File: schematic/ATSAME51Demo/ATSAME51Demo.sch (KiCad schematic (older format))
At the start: 1 part

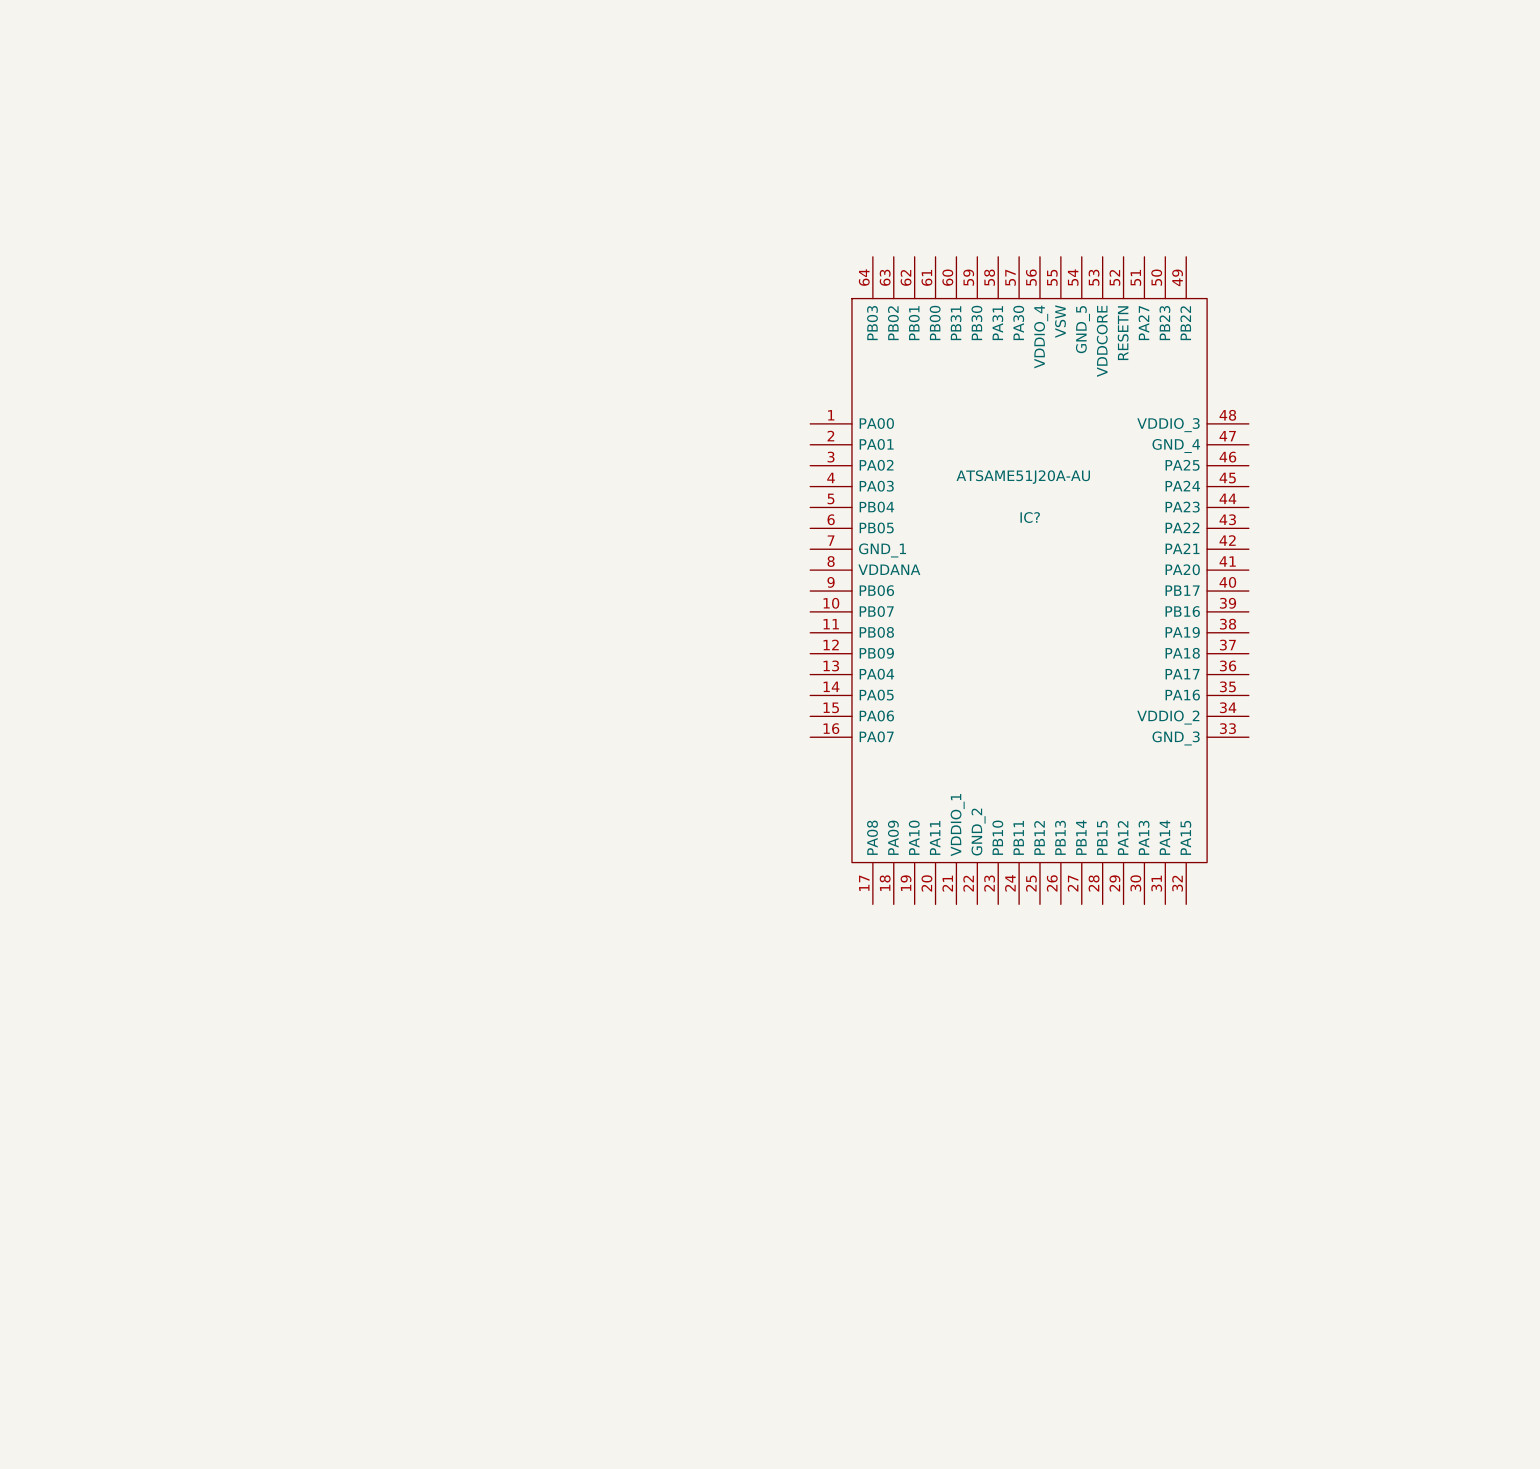
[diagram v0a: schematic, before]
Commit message: Schematic first draft
Still needs footprints
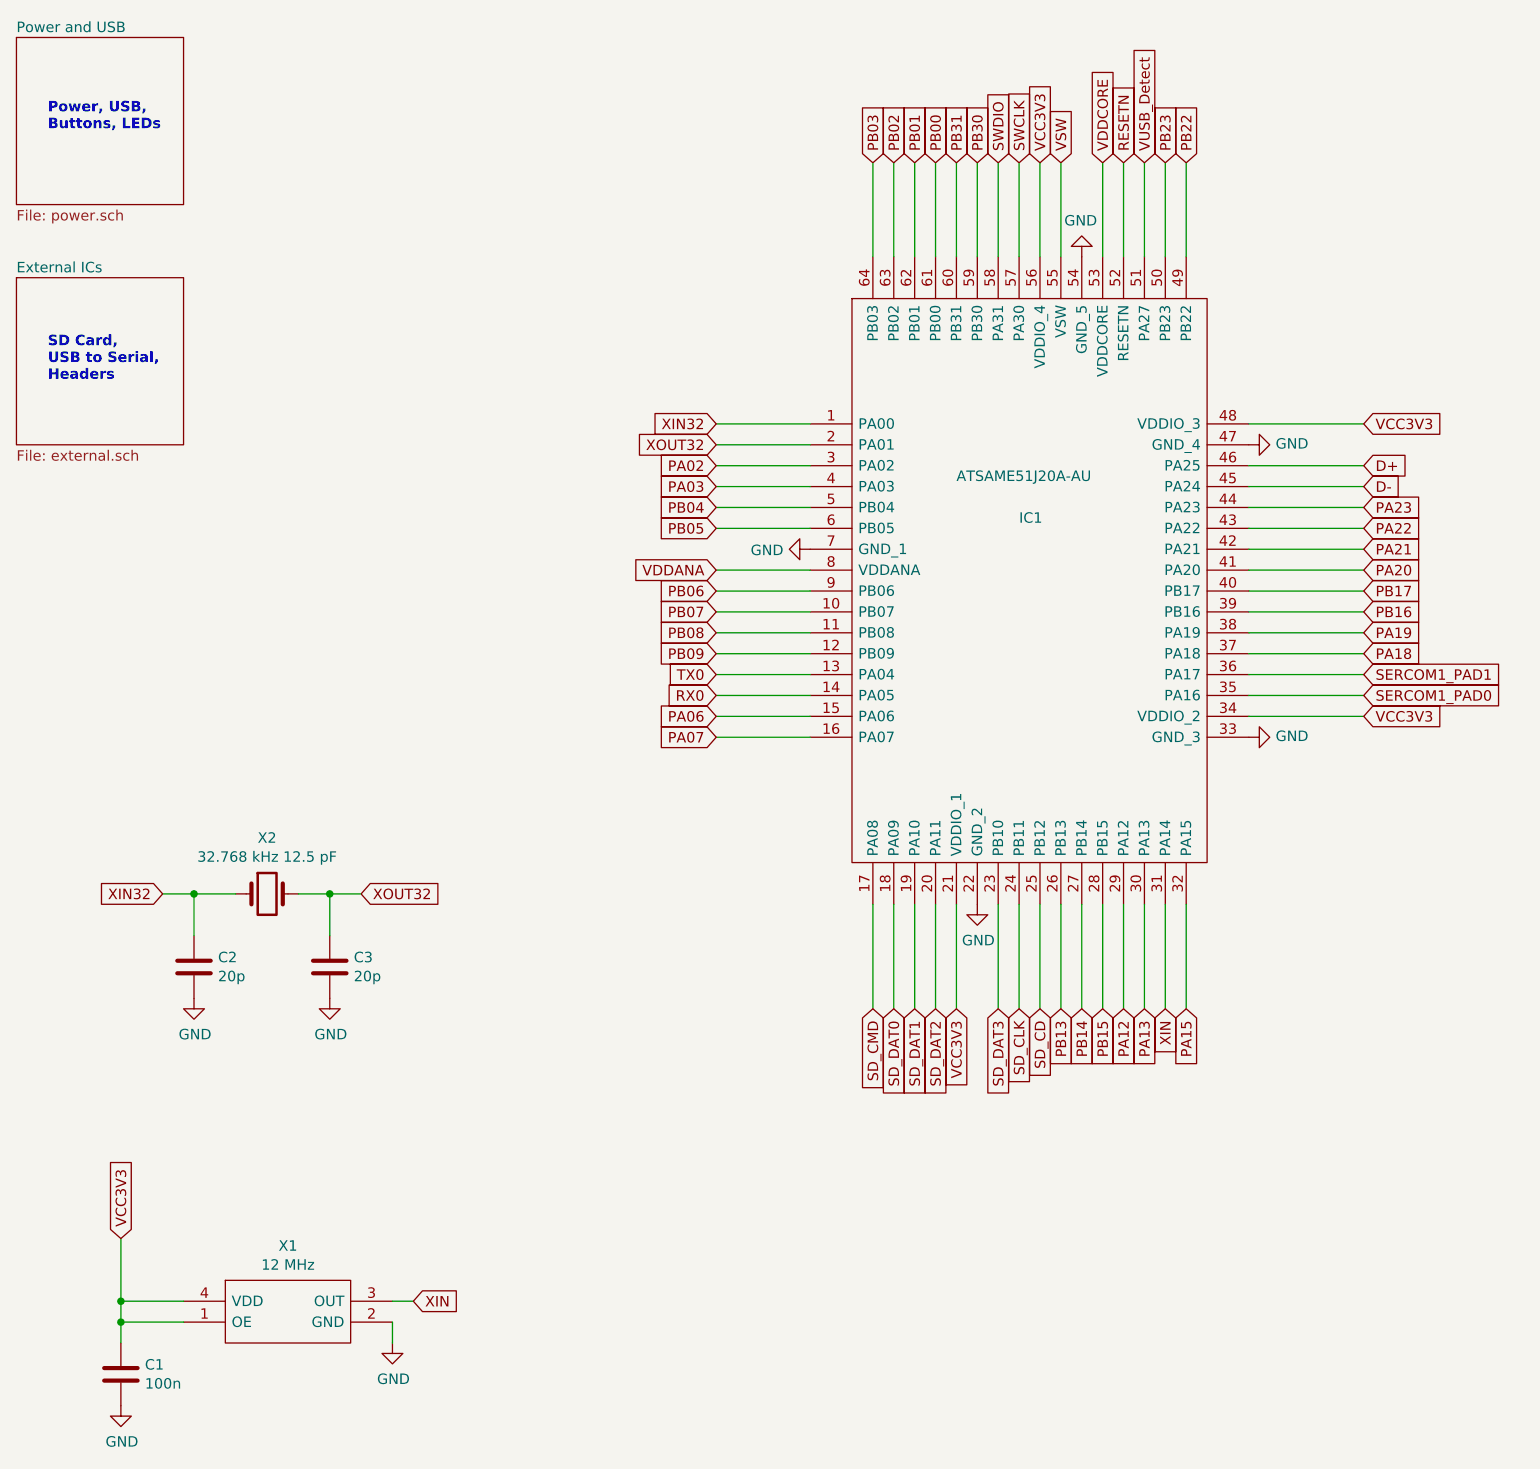
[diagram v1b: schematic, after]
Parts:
- added C1: 100n, symbol Device:C
- added C2, C3: 20p, symbol Device:C
- added X1: 12 MHz, SamacSys_Parts:ASTMUPCE3312000MHZLJET, symbol SamacSys_Parts:ASTMUPCE-33-12.000MHZ-LJ-E-T
- added X2: 32.768 kHz 12.5 pF, SamacSys_Parts:CM9VT1A, symbol Device:Crystal
- gave numbers to parts that had none: 1
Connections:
- net XIN32: now reaches IC1.1 (PA00)
- net XIN32: now also C2.1, X2.1
- net PB07: now reaches IC1.10 (PB07)
- net PB08: now reaches IC1.11 (PB08)
- net PB09: now reaches IC1.12 (PB09)
- net TX0: now reaches IC1.13 (PA04)
- net RX0: now reaches IC1.14 (PA05)
- net PA06: now reaches IC1.15 (PA06)
- net PA07: now reaches IC1.16 (PA07)
- net SD_CMD: now reaches IC1.17 (PA08)
- net SD_DAT0: now reaches IC1.18 (PA09)
- net SD_DAT1: now reaches IC1.19 (PA10)
- net XOUT32: now reaches IC1.2 (PA01)
- net XOUT32: now also C3.1, X2.2
- net SD_DAT2: now reaches IC1.20 (PA11)
- net VCC3V3: now reaches IC1.21 (VDDIO_1)
- net VCC3V3: now also IC1.34 (VDDIO_2), IC1.48 (VDDIO_3), IC1.56 (VDDIO_4), C1.1, X1.1 (OE), X1.4 (VDD)
- net GND: now reaches IC1.22 (GND_2)
- net GND: now also IC1.33 (GND_3), IC1.47 (GND_4), IC1.54 (GND_5), IC1.7 (GND_1), C1.2, C2.2, C3.2, X1.2 (GND)
- net SD_DAT3: now reaches IC1.23 (PB10)
- net SD_CLK: now reaches IC1.24 (PB11)
- net SD_CD: now reaches IC1.25 (PB12)
- net PB13: now reaches IC1.26 (PB13)
- net PB14: now reaches IC1.27 (PB14)
- net PB15: now reaches IC1.28 (PB15)
- net PA12: now reaches IC1.29 (PA12)
- net PA02: now reaches IC1.3 (PA02)
- net PA13: now reaches IC1.30 (PA13)
- net XIN: now reaches IC1.31 (PA14)
- net XIN: now also X1.3 (OUT)
- net PA15: now reaches IC1.32 (PA15)
- net SERCOM1_PAD0: now reaches IC1.35 (PA16)
- net SERCOM1_PAD1: now reaches IC1.36 (PA17)
- net PA18: now reaches IC1.37 (PA18)
- net PA19: now reaches IC1.38 (PA19)
- net PB16: now reaches IC1.39 (PB16)
- net PA03: now reaches IC1.4 (PA03)
- net PB17: now reaches IC1.40 (PB17)
- net PA20: now reaches IC1.41 (PA20)
- net PA21: now reaches IC1.42 (PA21)
- net PA22: now reaches IC1.43 (PA22)
- net PA23: now reaches IC1.44 (PA23)
- net D-: now reaches IC1.45 (PA24)
- net D+: now reaches IC1.46 (PA25)
- net PB22: now reaches IC1.49 (PB22)
- net PB04: now reaches IC1.5 (PB04)
- net PB23: now reaches IC1.50 (PB23)
- net VUSB_Detect: now reaches IC1.51 (PA27)
- net RESETN: now reaches IC1.52 (RESETN)
- net VDDCORE: now reaches IC1.53 (VDDCORE)
- net VSW: now reaches IC1.55 (VSW)
- net SWCLK: now reaches IC1.57 (PA30)
- net SWDIO: now reaches IC1.58 (PA31)
- net PB30: now reaches IC1.59 (PB30)
- net PB05: now reaches IC1.6 (PB05)
- net PB31: now reaches IC1.60 (PB31)
- net PB00: now reaches IC1.61 (PB00)
- net PB01: now reaches IC1.62 (PB01)
- net PB02: now reaches IC1.63 (PB02)
- net PB03: now reaches IC1.64 (PB03)
- net VDDANA: now reaches IC1.8 (VDDANA)
- net PB06: now reaches IC1.9 (PB06)
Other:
- note added: "Power, USB, \nButtons, LEDs"
- note added: "SD Card, \nUSB to Serial,\nHeaders"

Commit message: Footprints assigned
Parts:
- C1: footprint (none) -> Capacitor_SMD:C_0402_1005Metric
- C2, C3: footprint (none) -> Capacitor_SMD:C_0603_1608Metric
- IC1: footprint QFP50P1200X1200X120-64N -> SamacSys_Parts:QFP50P1200X1200X120-64N
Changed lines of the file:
@@
 F 0 "IC1" H 5450 2200 50  0000 L CNN
 F 1 "ATSAME51J20A-AU" H 5150 2400 50  0000 L CNN
-F 2 "QFP50P1200X1200X120-64N" H 6400 3250 50  0001 L CNN
+F 2 "SamacSys_Parts:QFP50P1200X1200X120-64N" H 6400 3250 50  0001 L CNN
 F 3 "http://ww1.microchip.com/downloads/en/DeviceDoc/SAM-D5xE5x-Family-Datasheet-01507B.pdf" H 6400 3150 50  0001 L CNN
 F 4 "MICROCHIP - ATSAME51J20A-AU - MCU, ARM CORTEX-M4F, 120MHZ, TQFP-64" H 6400 3050 50  0001 L CNN "Description"
@@
 F 0 "C2" H 1615 5296 50  0000 L CNN
 F 1 "20p" H 1615 5205 50  0000 L CNN
-F 2 "" H 1538 5100 50  0001 C CNN
+F 2 "Capacitor_SMD:C_0603_1608Metric" H 1538 5100 50  0001 C CNN
 F 3 "~" H 1500 5250 50  0001 C CNN
 	1    1500 5250
@@
 F 0 "C3" H 2265 5296 50  0000 L CNN
 F 1 "20p" H 2265 5205 50  0000 L CNN
-F 2 "" H 2188 5100 50  0001 C CNN
+F 2 "Capacitor_SMD:C_0603_1608Metric" H 2188 5100 50  0001 C CNN
 F 3 "~" H 2150 5250 50  0001 C CNN
 	1    2150 5250
@@
 F 0 "C1" H 1265 7246 50  0000 L CNN
 F 1 "100n" H 1265 7155 50  0000 L CNN
-F 2 "" H 1188 7050 50  0001 C CNN
+F 2 "Capacitor_SMD:C_0402_1005Metric" H 1188 7050 50  0001 C CNN
 F 3 "~" H 1150 7200 50  0001 C CNN
 	1    1150 7200

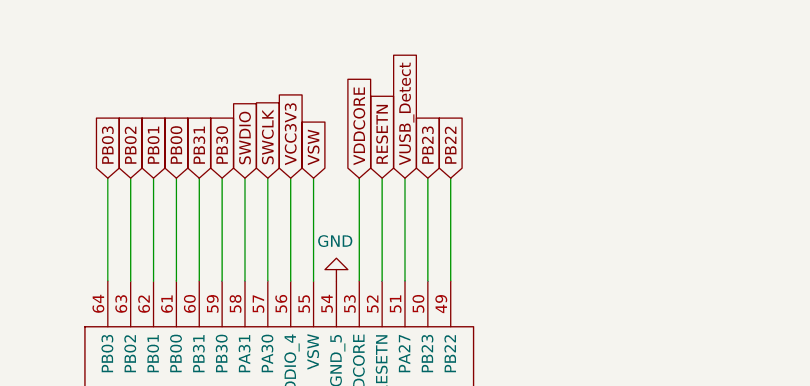
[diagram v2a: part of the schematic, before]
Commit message: Removed USB detect
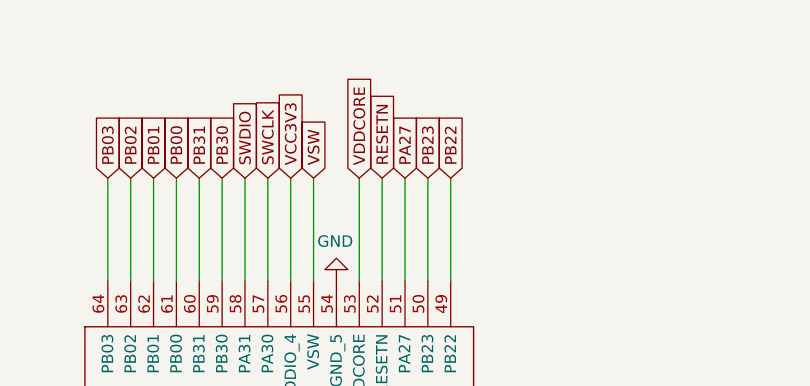
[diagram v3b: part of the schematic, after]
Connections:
- net VUSB_Detect renamed PA27
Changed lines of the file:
@@
 Sheet 1 3
 Title "ATSAME51 Demo Board"
-Date ""
+Date "2021-10-25"
 Rev "1.0"
 Comp "Quantum Embedded Systems"
@@
 PB23
 Text GLabel 6050 1400 1    50   Input ~ 0
-VUSB_Detect
+PA27
 Text GLabel 5250 1400 1    50   Input ~ 0
 PB30
